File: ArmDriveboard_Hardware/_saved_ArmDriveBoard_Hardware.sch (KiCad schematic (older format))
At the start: 38 parts, among them Q1 Q_NMOS_GSD, Q2 Q_NMOS_GSD, U1 TM4C129E_Launchpad, U3 OKI

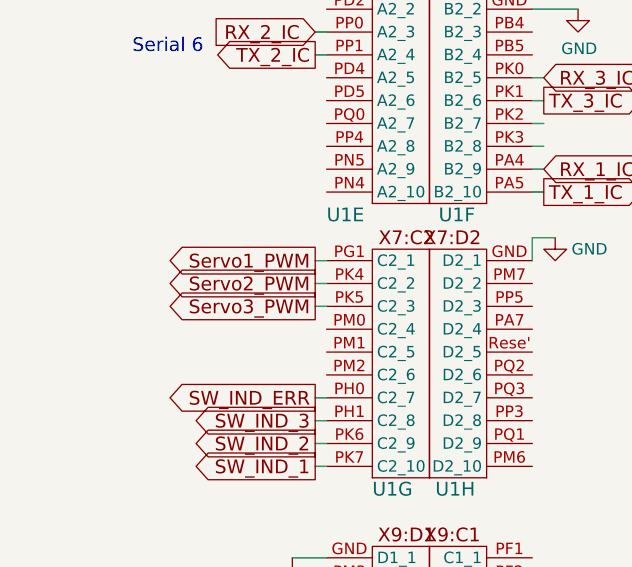
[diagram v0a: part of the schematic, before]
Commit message: fix for Rev 3 driveboard
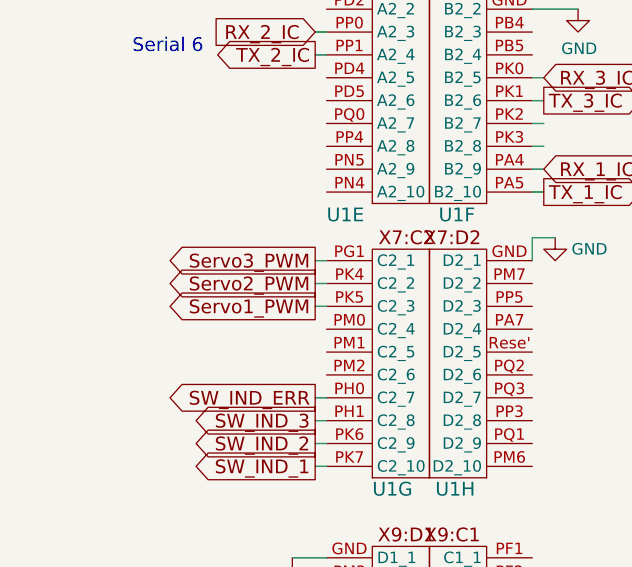
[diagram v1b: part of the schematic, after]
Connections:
- net Servo1_PWM: now also U1.PK5 (C2_3); no longer U1.PG1 (C2_1)
- net Servo3_PWM: now also U1.PG1 (C2_1); no longer U1.PK5 (C2_3)
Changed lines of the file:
@@
 Text GLabel 7150 2100 0    60   Input ~ 0
 Servo2_PWM
-Text GLabel 1750 4650 0    60   Output ~ 0
+Text GLabel 1750 4850 0    60   Output ~ 0
 Servo1_PWM
 $Comp
@@
 Text GLabel 1750 4750 0    60   Output ~ 0
 Servo2_PWM
-Text GLabel 1750 4850 0    60   Output ~ 0
+Text GLabel 1750 4650 0    60   Output ~ 0
 Servo3_PWM
 $Comp

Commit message: made rev 2
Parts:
- added Conn1: AndersonPP, MRDT_Connectors:Anderson_3_Vertical_Side_by_Side, symbol ArmDriveBoard_Hardware-rescue:AndersonPP-MRDT_Connectors-ArmDriveBoard_Hardware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
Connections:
- net +12V: now also Conn1.3 (V+Act); no longer Conn6.1, R3.1
- net GND: now also Conn1.1 (GND)
- net V+Log: now also Conn1.2 (V+Log)
- new net +24V: Conn6.1, R3.1
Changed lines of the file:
@@
-$EndComp
-$Comp
-L power:+12V #PWR0112
-U 1 1 5CB9F541
-P 9300 1250
-F 0 "#PWR0112" H 9300 1100 50  0001 C CNN
-F 1 "+12V" H 9315 1423 50  0000 C CNN
-F 2 "" H 9300 1250 50  0001 C CNN
-F 3 "" H 9300 1250 50  0001 C CNN
-	1    9300 1250
-	1    0    0    -1
 $EndComp
 $Comp
@@
 Wire Wire Line
 	10200 1050 10450 1050
+$Comp
+L power:+24V #PWR0112
+U 1 1 5CC3F2F4
+P 9300 1250
+F 0 "#PWR0112" H 9300 1100 50  0001 C CNN
+F 1 "+24V" H 9315 1423 50  0000 C CNN
+F 2 "" H 9300 1250 50  0001 C CNN
+F 3 "" H 9300 1250 50  0001 C CNN
+	1    9300 1250
+	1    0    0    -1
+$EndComp
+$Comp
+L ArmDriveBoard_Hardware-rescue:AndersonPP-MRDT_Connectors-ArmDriveBoard_Hardware-rescue Conn1
+U 2 1 5CC3F71A
+P 100 2000
+F 0 "Conn1" H 150 2250 60  0000 C CNN
+F 1 "AndersonPP" H -150 2100 60  0001 C CNN
+F 2 "MRDT_Connectors:Anderson_3_Vertical_Side_by_Side" H -50 1450 60  0001 C CNN
+F 3 "" H -50 1450 60  0001 C CNN
+	2    100  2000
+	1    0    0    -1
+$EndComp
+$Comp
+L ArmDriveBoard_Hardware-rescue:AndersonPP-MRDT_Connectors-ArmDriveBoard_Hardware-rescue Conn1
+U 1 1 5CC3F720
+P 100 2300
+F 0 "Conn1" H 150 2250 60  0000 C CNN
+F 1 "AndersonPP" H -150 2400 60  0001 C CNN
+F 2 "MRDT_Connectors:Anderson_3_Vertical_Side_by_Side" H -50 1750 60  0001 C CNN
+F 3 "" H -50 1750 60  0001 C CNN
+	1    100  2300
+	1    0    0    -1
+$EndComp
+$Comp
+L ArmDriveBoard_Hardware-rescue:AndersonPP-MRDT_Connectors-ArmDriveBoard_Hardware-rescue Conn1
+U 3 1 5CC3F726
+P 100 1650
+F 0 "Conn1" H 150 1900 60  0000 C CNN
+F 1 "AndersonPP" H 350 2050 60  0001 C CNN
+F 2 "MRDT_Connectors:Anderson_3_Vertical_Side_by_Side" H -50 1100 60  0001 C CNN
+F 3 "" H -50 1100 60  0001 C CNN
+	3    100  1650
+	1    0    0    -1
+$EndComp
+Text Notes 100  1300 0    79   ~ 0
+Vin
+Wire Wire Line
+	500  1550 1050 1550
+Connection ~ 1050 1550
+Connection ~ 1050 1900
+Connection ~ 1050 2200
+Wire Wire Line
+	500  1900 1050 1900
+Wire Wire Line
+	500  2200 1050 2200
 $EndSCHEMATC
